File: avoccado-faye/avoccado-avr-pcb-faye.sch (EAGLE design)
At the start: 57 parts, among them Q1 16MHz, Q2 FET, U2 MCP73831

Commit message: add test points
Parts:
- added JP16: M01SMD-4.5X1.5, SparkFun-Connectors:M01SMD-4.5X1.5
- added TP3, TP5: TEST-POINT3X5, SparkFun-Passives:TEST-POINT3X5
- added TP4: TEST-POINT3, SparkFun-Passives:TEST-POINT3
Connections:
- net 3.3V: now also TP5.1
- net 5V: now also TP4.1
- net GND: now also TP3.1
- net VIBR: now also JP16.1
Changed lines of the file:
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@@
 <setting verticaltext="up"/>
 </settings>
-<grid distance="0.1" unitdist="inch" unit="inch" style="lines" multiple="1" display="no" altdistance="0.01" altunitdist="inch" altunit="inch"/>
+<grid distance="20" unitdist="mil" unit="mil" style="lines" multiple="1" display="yes" altdistance="0.01" altunitdist="inch" altunit="inch"/>
 <layers>
 <layer number="1" name="Top" color="4" fill="1" visible="no" active="no"/>
@@
 <part name="R12" library="SparkFun-Resistors" deviceset="RESISTOR" device="0402" value="1K"/>
 <part name="R9" library="SparkFun-Resistors" deviceset="RESISTOR" device="0402" value="1K"/>
+<part name="TP5" library="SparkFun-Passives" deviceset="TEST-POINT" device="3X5"/>
+<part name="TP3" library="SparkFun-Passives" deviceset="TEST-POINT" device="3X5"/>
+<part name="TP4" library="SparkFun-Passives" deviceset="TEST-POINT" device="3"/>
+<part name="JP16" library="SparkFun-Connectors" deviceset="M01" device="SMD-4.5X1.5"/>
 </parts>
 <sheets>
@@
 <instance part="R12" gate="G$1" x="81.28" y="160.02" rot="R90"/>
 <instance part="R9" gate="G$1" x="81.28" y="147.32" rot="R90"/>
+<instance part="TP5" gate="G$1" x="99.06" y="119.38"/>
+<instance part="TP3" gate="G$1" x="99.06" y="103.124"/>
+<instance part="TP4" gate="G$1" x="18.288" y="177.8" rot="R180"/>
+<instance part="JP16" gate="G$1" x="383.54" y="116.84" rot="R180"/>
 </instances>
 <busses>
@@
 </segment>
 <segment>
-<wire x1="78.74" y1="101.6" x2="78.74" y2="104.14" width="0.1524" layer="91"/>
+<wire x1="78.74" y1="101.6" x2="78.74" y2="103.124" width="0.1524" layer="91"/>
 <pinref part="C10" gate="G$1" pin="2"/>
 <pinref part="GND26" gate="1" pin="GND"/>
+<pinref part="TP3" gate="G$1" pin="1"/>
+<wire x1="78.74" y1="103.124" x2="78.74" y2="104.14" width="0.1524" layer="91"/>
+<wire x1="99.06" y1="103.124" x2="78.74" y2="103.124" width="0.1524" layer="91"/>
+<junction x="78.74" y="103.124"/>
 </segment>
 <segment>
@@
 <wire x1="71.12" y1="114.3" x2="78.74" y2="114.3" width="0.1524" layer="91"/>
 <wire x1="78.74" y1="114.3" x2="91.44" y2="114.3" width="0.1524" layer="91"/>
-<wire x1="91.44" y1="114.3" x2="91.44" y2="124.46" width="0.1524" layer="91"/>
+<wire x1="91.44" y1="114.3" x2="91.44" y2="119.38" width="0.1524" layer="91"/>
+<wire x1="91.44" y1="119.38" x2="91.44" y2="124.46" width="0.1524" layer="91"/>
 <wire x1="78.74" y1="114.3" x2="78.74" y2="111.76" width="0.1524" layer="91"/>
 <wire x1="71.12" y1="114.3" x2="71.12" y2="111.76" width="0.1524" layer="91"/>
@@
 <junction x="68.58" y="114.3"/>
 <pinref part="C6" gate="G$1" pin="1"/>
+<pinref part="TP5" gate="G$1" pin="1"/>
+<wire x1="91.44" y1="119.38" x2="99.06" y2="119.38" width="0.1524" layer="91"/>
+<junction x="91.44" y="119.38"/>
 </segment>
 <segment>
@@
 <wire x1="22.86" y1="170.18" x2="25.4" y2="170.18" width="0.1524" layer="91"/>
 <junction x="25.4" y="170.18"/>
+<pinref part="TP4" gate="G$1" pin="1"/>
+<wire x1="18.288" y1="177.8" x2="25.4" y2="177.8" width="0.1524" layer="91"/>
+<wire x1="25.4" y1="177.8" x2="25.4" y2="170.18" width="0.1524" layer="91"/>
 </segment>
 <segment>
@@
 </segment>
 <segment>
-<wire x1="375.92" y1="127" x2="350.52" y2="127" width="0.2032" layer="91"/>
+<wire x1="375.92" y1="127" x2="365.76" y2="127" width="0.2032" layer="91"/>
 <pinref part="JP23" gate="G$1" pin="1"/>
 <label x="350.52" y="127" size="1.778" layer="95"/>
-</segment>
-</net>
+<pinref part="JP16" gate="G$1" pin="1"/>
+<wire x1="365.76" y1="127" x2="350.52" y2="127" width="0.2032" layer="91"/>
+<wire x1="375.92" y1="116.84" x2="365.76" y2="116.84" width="0.1524" layer="91"/>
+<wire x1="365.76" y1="116.84" x2="365.76" y2="127" width="0.1524" layer="91"/>
+<junction x="365.76" y="127"/>
+</segment>
+</net>

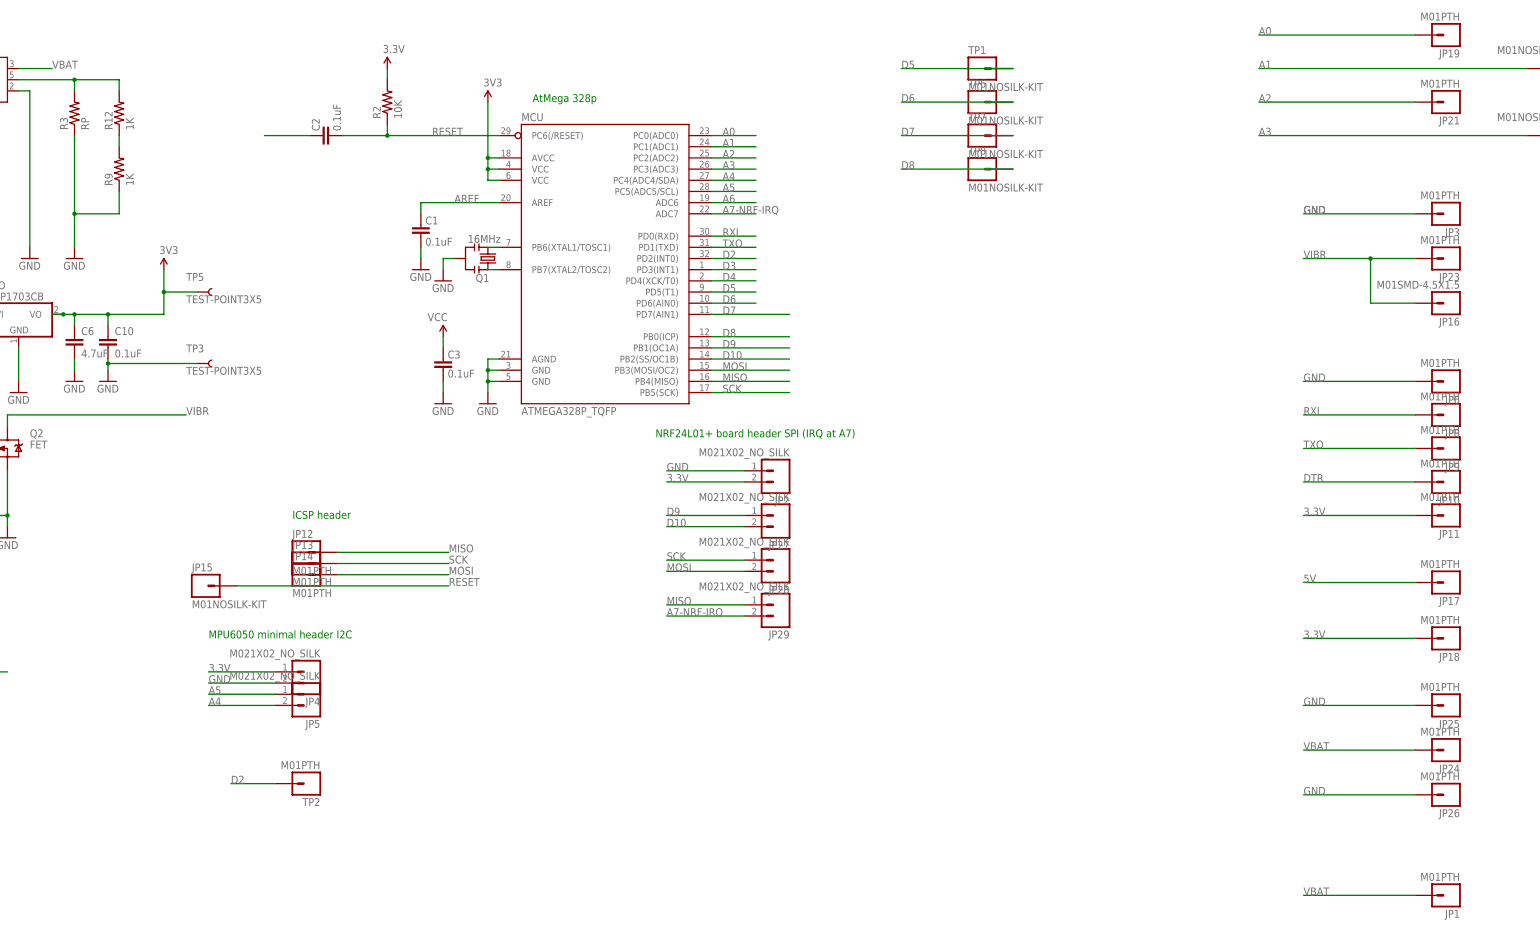
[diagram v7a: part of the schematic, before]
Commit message: new: all headers on 100mil grid
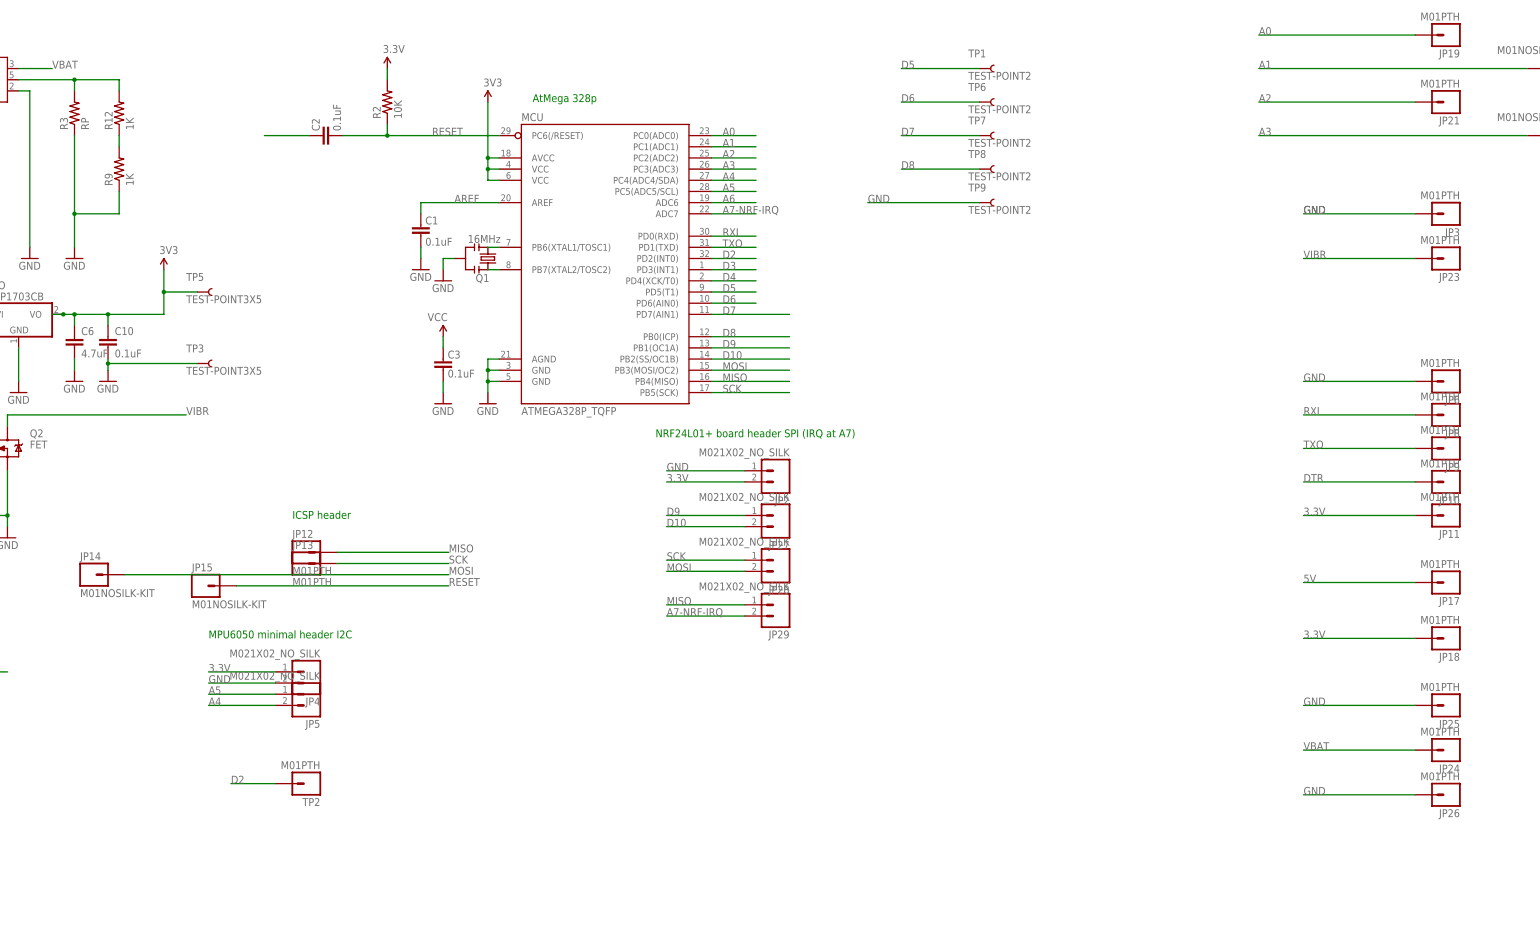
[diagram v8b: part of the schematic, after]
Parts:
- removed JP1: M01PTH, SparkFun-Connectors:M01PTH
- removed JP16: M01SMD-4.5X1.5, SparkFun-Connectors:M01SMD-4.5X1.5
- added TP9: TEST-POINT2, SparkFun-Passives:TEST-POINT2
- JP14: value M01PTH -> M01NOSILK-KIT; device SparkFun-Connectors:M01PTH -> SparkFun-Connectors:M01NOSILK-KIT
- TP1, TP6, TP7, TP8: value M01NOSILK-KIT -> TEST-POINT2; device SparkFun-Connectors:M01NOSILK-KIT -> SparkFun-Passives:TEST-POINT2
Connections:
- net GND: now also TP9.1
- net VBAT: no longer JP1.1
- net VIBR: no longer JP16.1
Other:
- moved on the sheet: JP14
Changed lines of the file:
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@@
 <setting verticaltext="up"/>
 </settings>
-<grid distance="20" unitdist="mil" unit="mil" style="lines" multiple="1" display="yes" altdistance="0.01" altunitdist="inch" altunit="inch"/>
+<grid distance="0.1" unitdist="inch" unit="inch" style="lines" multiple="1" display="no" altdistance="0.01" altunitdist="inch" altunit="inch"/>
 <layers>
 <layer number="1" name="Top" color="4" fill="1" visible="no" active="no"/>
@@
 <part name="JP12" library="SparkFun-Connectors" deviceset="M01" device="PTH" value="M01PTH"/>
 <part name="JP13" library="SparkFun-Connectors" deviceset="M01" device="PTH" value="M01PTH"/>
-<part name="JP14" library="SparkFun-Connectors" deviceset="M01" device="PTH" value="M01PTH"/>
+<part name="JP14" library="SparkFun-Connectors" deviceset="M01" device="NOSILK-KIT" value="M01NOSILK-KIT"/>
 <part name="JP15" library="SparkFun-Connectors" deviceset="M01" device="NOSILK-KIT" value="M01NOSILK-KIT"/>
 <part name="JP3" library="SparkFun-Connectors" deviceset="M01" device="PTH" value="M01PTH"/>
@@
 <part name="JP18" library="SparkFun-Connectors" deviceset="M01" device="PTH" value="M01PTH"/>
 <part name="C2" library="SparkFun" deviceset="CAP" device="0402" value="0.1uF"/>
-<part name="TP1" library="SparkFun-Connectors" deviceset="M01" device="NOSILK-KIT"/>
-<part name="TP6" library="SparkFun-Connectors" deviceset="M01" device="NOSILK-KIT"/>
-<part name="TP7" library="SparkFun-Connectors" deviceset="M01" device="NOSILK-KIT"/>
-<part name="TP8" library="SparkFun-Connectors" deviceset="M01" device="NOSILK-KIT"/>
+<part name="TP1" library="SparkFun-Passives" deviceset="TEST-POINT" device="2"/>
+<part name="TP6" library="SparkFun-Passives" deviceset="TEST-POINT" device="2"/>
+<part name="TP7" library="SparkFun-Passives" deviceset="TEST-POINT" device="2"/>
+<part name="TP8" library="SparkFun-Passives" deviceset="TEST-POINT" device="2"/>
 <part name="JP19" library="SparkFun-Connectors" deviceset="M01" device="PTH" value="M01PTH"/>
 <part name="JP20" library="SparkFun-Connectors" deviceset="M01" device="NOSILK-KIT" value="M01NOSILK-KIT"/>
@@
 <part name="C7" library="SparkFun" deviceset="CAP" device="0402" value="0.1uF"/>
 <part name="GND10" library="SparkFun" deviceset="GND" device=""/>
-<part name="JP1" library="SparkFun-Connectors" deviceset="M01" device="PTH" value="M01PTH"/>
 <part name="MCU" library="SparkFun-DigitalIC" deviceset="ATMEGA328P_TQFP" device="" value="ATMEGA328P_TQFP"/>
 <part name="JP7" library="SparkFun-Connectors" deviceset="USB" device="-MICROB"/>
@@
 <part name="TP3" library="SparkFun-Passives" deviceset="TEST-POINT" device="3X5"/>
 <part name="TP4" library="SparkFun-Passives" deviceset="TEST-POINT" device="3"/>
-<part name="JP16" library="SparkFun-Connectors" deviceset="M01" device="SMD-4.5X1.5"/>
+<part name="TP9" library="SparkFun-Passives" deviceset="TEST-POINT" device="2"/>
 </parts>
 <sheets>
@@
 <instance part="JP12" gate="G$1" x="123.19" y="60.198"/>
 <instance part="JP13" gate="G$1" x="123.19" y="57.658"/>
-<instance part="JP14" gate="G$1" x="123.19" y="55.118"/>
+<instance part="JP14" gate="G$1" x="74.93" y="55.118"/>
 <instance part="JP15" gate="G$1" x="100.33" y="52.578"/>
 <instance part="JP3" gate="G$1" x="383.54" y="137.16" rot="R180"/>
@@
 <instance part="C7" gate="G$1" x="30.48" y="25.4"/>
 <instance part="GND10" gate="1" x="20.32" y="12.7"/>
-<instance part="JP1" gate="G$1" x="383.54" y="-17.78" rot="R180"/>
 <instance part="MCU" gate="U$1" x="193.04" y="124.46"/>
 <instance part="JP7" gate="G$1" x="12.7" y="165.1" rot="R180"/>
@@
 <instance part="TP3" gate="G$1" x="99.06" y="103.124"/>
 <instance part="TP4" gate="G$1" x="18.288" y="177.8" rot="R180"/>
-<instance part="JP16" gate="G$1" x="383.54" y="116.84" rot="R180"/>
+<instance part="TP9" gate="G$1" x="276.86" y="139.7"/>
 </instances>
 <busses>
@@
 <pinref part="JP3" gate="G$1" pin="1"/>
 <label x="350.52" y="137.16" size="1.778" layer="95"/>
+<label x="251.46" y="139.7" size="1.778" layer="95"/>
 </segment>
 <segment>
@@
 <junction x="20.32" y="17.78"/>
 </segment>
+<segment>
+<wire x1="276.86" y1="139.7" x2="251.46" y2="139.7" width="0.1524" layer="91"/>
+<pinref part="TP9" gate="G$1" pin="1"/>
+</segment>
 </net>
 <net name="AREF" class="0">
@@
 </segment>
 <segment>
-<wire x1="156.21" y1="55.118" x2="130.81" y2="55.118" width="0.1524" layer="91"/>
+<wire x1="156.21" y1="55.118" x2="82.55" y2="55.118" width="0.1524" layer="91"/>
 <pinref part="JP14" gate="G$1" pin="1"/>
 <label x="156.21" y="55.118" size="1.778" layer="95"/>
@@
 </segment>
 <segment>
-<wire x1="259.08" y1="147.32" x2="284.48" y2="147.32" width="0.1524" layer="91"/>
+<wire x1="259.08" y1="147.32" x2="276.86" y2="147.32" width="0.1524" layer="91"/>
 <pinref part="TP8" gate="G$1" pin="1"/>
 <label x="259.08" y="147.32" size="1.778" layer="95"/>
@@
 </segment>
 <segment>
-<wire x1="259.08" y1="170.18" x2="284.48" y2="170.18" width="0.1524" layer="91"/>
+<wire x1="259.08" y1="170.18" x2="276.86" y2="170.18" width="0.1524" layer="91"/>
 <pinref part="TP1" gate="G$1" pin="1"/>
 <label x="259.08" y="170.18" size="1.778" layer="95"/>
@@
 </segment>
 <segment>
-<wire x1="259.08" y1="162.56" x2="284.48" y2="162.56" width="0.1524" layer="91"/>
+<wire x1="259.08" y1="162.56" x2="276.86" y2="162.56" width="0.1524" layer="91"/>
 <pinref part="TP6" gate="G$1" pin="1"/>
 <label x="259.08" y="162.56" size="1.778" layer="95"/>
@@
 </segment>
 <segment>
-<wire x1="259.08" y1="154.94" x2="284.48" y2="154.94" width="0.1524" layer="91"/>
+<wire x1="259.08" y1="154.94" x2="276.86" y2="154.94" width="0.1524" layer="91"/>
 <pinref part="TP7" gate="G$1" pin="1"/>
 <label x="259.08" y="154.94" size="1.778" layer="95"/>
@@
 </segment>
 <segment>
-<wire x1="375.92" y1="127" x2="365.76" y2="127" width="0.2032" layer="91"/>
 <pinref part="JP23" gate="G$1" pin="1"/>
 <label x="350.52" y="127" size="1.778" layer="95"/>
-<pinref part="JP16" gate="G$1" pin="1"/>
-<wire x1="365.76" y1="127" x2="350.52" y2="127" width="0.2032" layer="91"/>
-<wire x1="375.92" y1="116.84" x2="365.76" y2="116.84" width="0.1524" layer="91"/>
-<wire x1="365.76" y1="116.84" x2="365.76" y2="127" width="0.1524" layer="91"/>
-<junction x="365.76" y="127"/>
+<wire x1="375.92" y1="127" x2="350.52" y2="127" width="0.2032" layer="91"/>
 </segment>
 </net>
@@
 <pinref part="R8" gate="G$1" pin="2"/>
 </segment>
-<segment>
-<wire x1="375.92" y1="-17.78" x2="350.52" y2="-17.78" width="0.1524" layer="91"/>
-<pinref part="JP1" gate="G$1" pin="1"/>
-<label x="350.52" y="-17.78" size="1.778" layer="95"/>
-</segment>
-</net>
+</net>
